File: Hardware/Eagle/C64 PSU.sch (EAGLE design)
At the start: 9 parts

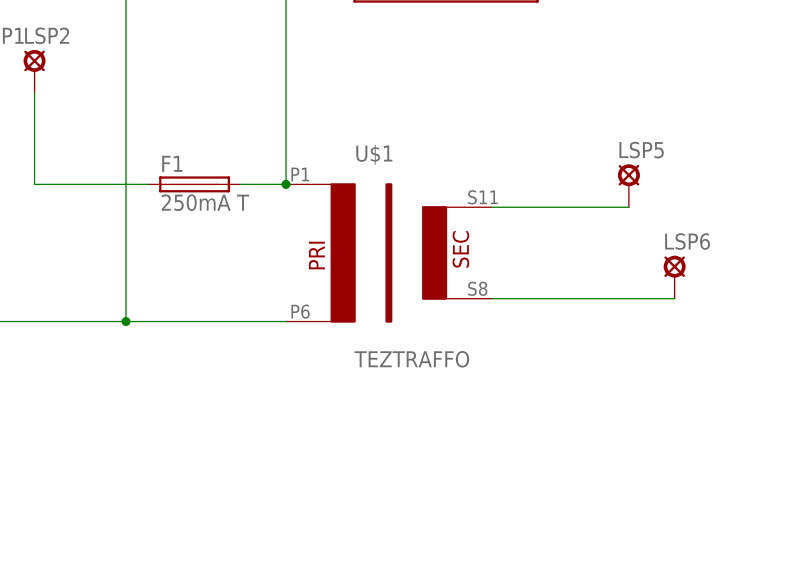
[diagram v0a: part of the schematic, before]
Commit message: Fixed solder pads for trafo
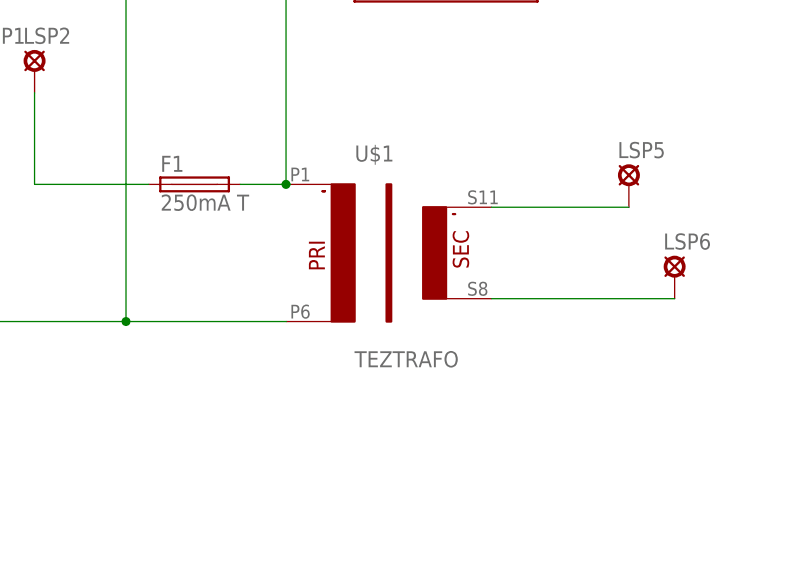
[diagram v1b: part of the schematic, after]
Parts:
- U$1: value TEZTRAFFO -> TEZTRAFO; device traffo:TEZTRAFFO -> trafo:TEZTRAFO
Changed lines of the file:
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@@
 <?xml version="1.0" encoding="utf-8"?>
 <!DOCTYPE eagle SYSTEM "eagle.dtd">
-<eagle version="9.1.3">
+<eagle version="9.2.2">
 <drawing>
 <settings>
@@
 </classes>
 <parts>
-<part name="U$1" library="traffo" deviceset="TEZTRAFFO" device=""/>
+<part name="U$1" library="trafo" deviceset="TEZTRAFO" device=""/>
 <part name="F1" library="fuse" library_urn="urn:adsk.eagle:library:233" deviceset="FUSE" device="SH22,5" package3d_urn="urn:adsk.eagle:package:14059/1" value="250mA T"/>
 <part name="FRAME1" library="frames" library_urn="urn:adsk.eagle:library:229" deviceset="A3L-LOC" device=""/>

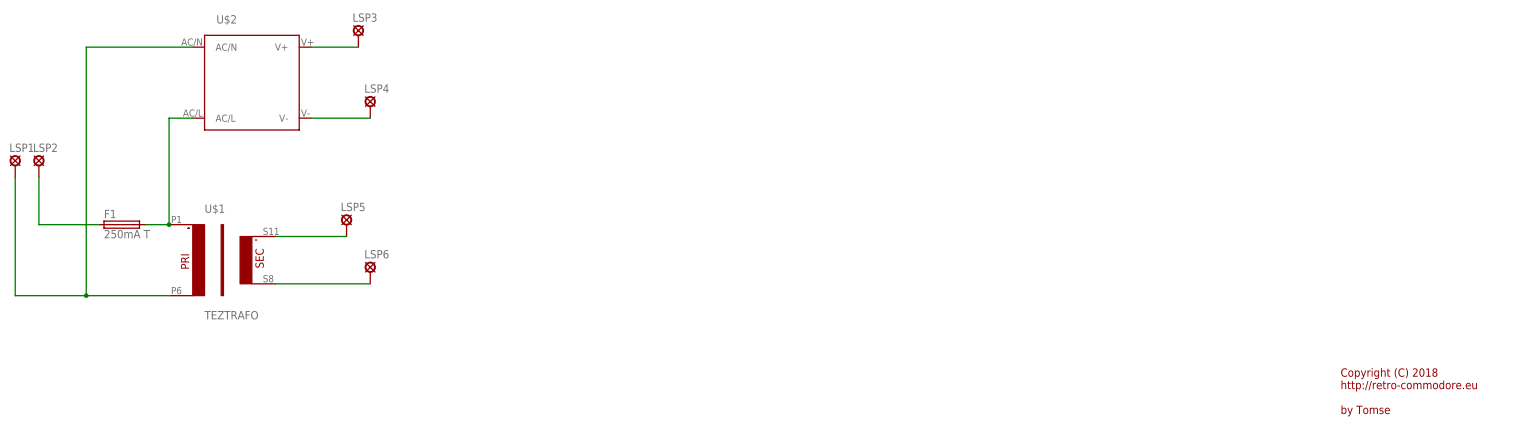
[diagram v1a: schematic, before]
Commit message: added power led connectors
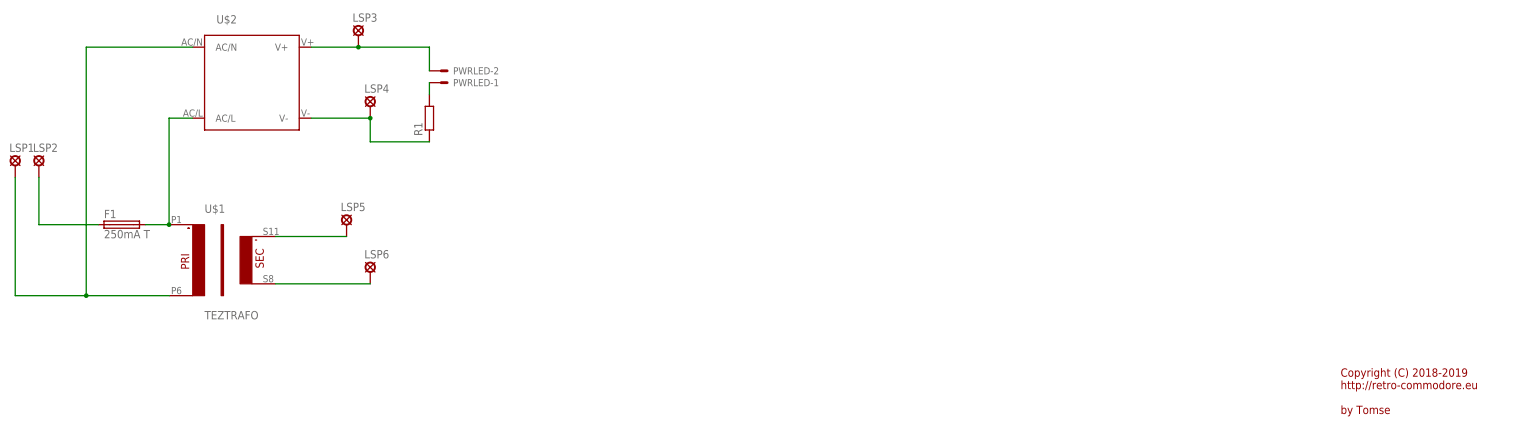
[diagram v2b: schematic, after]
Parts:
- added PWRLED: 22-23-2021, con-molex:22-23-2021
- added R1: (no value), rcl:R-EU_0207/10
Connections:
- new net N$8: PWRLED-1.S, R1.2
- net N$6: now also R1.1
- net N$7: now also PWRLED-2.S
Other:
- note added: "Copyright (C) 2018-2019 http://retro-commodore.eu by Tomse"
- note removed: "Copyright (C) 2018 http://retro-commodore.eu by Tomse"
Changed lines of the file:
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@@
 <?xml version="1.0" encoding="utf-8"?>
 <!DOCTYPE eagle SYSTEM "eagle.dtd">
-<eagle version="9.2.2">
+<eagle version="9.3.2">
 <drawing>
 <settings>
@@
 <grid distance="0.1" unitdist="inch" unit="inch" style="lines" multiple="1" display="no" altdistance="0.01" altunitdist="inch" altunit="inch"/>
 <layers>
-<layer number="1" name="Top" color="4" fill="1" visible="no" active="no"/>
-<layer number="16" name="Bottom" color="1" fill="1" visible="no" active="no"/>
-<layer number="17" name="Pads" color="2" fill="1" visible="no" active="no"/>
-<layer number="18" name="Vias" color="2" fill="1" visible="no" active="no"/>
-<layer number="19" name="Unrouted" color="6" fill="1" visible="no" active="no"/>
-<layer number="20" name="Dimension" color="24" fill="1" visible="no" active="no"/>
-<layer number="21" name="tPlace" color="7" fill="1" visible="no" active="no"/>
-<layer number="22" name="bPlace" color="7" fill="1" visible="no" active="no"/>
-<layer number="23" name="tOrigins" color="15" fill="1" visible="no" active="no"/>
-<layer number="24" name="bOrigins" color="15" fill="1" visible="no" active="no"/>
-<layer number="25" name="tNames" color="7" fill="1" visible="no" active="no"/>
-<layer number="26" name="bNames" color="7" fill="1" visible="no" active="no"/>
-<layer number="27" name="tValues" color="7" fill="1" visible="no" active="no"/>
-<layer number="28" name="bValues" color="7" fill="1" visible="no" active="no"/>
+<layer number="1" name="Top" color="4" fill="1" visible="yes" active="no"/>
+<layer number="16" name="Bottom" color="1" fill="1" visible="yes" active="no"/>
+<layer number="17" name="Pads" color="2" fill="1" visible="yes" active="no"/>
+<layer number="18" name="Vias" color="2" fill="1" visible="yes" active="no"/>
+<layer number="19" name="Unrouted" color="6" fill="1" visible="yes" active="no"/>
+<layer number="20" name="Dimension" color="24" fill="1" visible="yes" active="no"/>
+<layer number="21" name="tPlace" color="7" fill="1" visible="yes" active="no"/>
+<layer number="22" name="bPlace" color="7" fill="1" visible="yes" active="no"/>
+<layer number="23" name="tOrigins" color="15" fill="1" visible="yes" active="no"/>
+<layer number="24" name="bOrigins" color="15" fill="1" visible="yes" active="no"/>
+<layer number="25" name="tNames" color="7" fill="1" visible="yes" active="no"/>
+<layer number="26" name="bNames" color="7" fill="1" visible="yes" active="no"/>
+<layer number="27" name="tValues" color="7" fill="1" visible="yes" active="no"/>
+<layer number="28" name="bValues" color="7" fill="1" visible="yes" active="no"/>
 <layer number="29" name="tStop" color="7" fill="3" visible="no" active="no"/>
 <layer number="30" name="bStop" color="7" fill="6" visible="no" active="no"/>
@@
 <layer number="35" name="tGlue" color="7" fill="4" visible="no" active="no"/>
 <layer number="36" name="bGlue" color="7" fill="5" visible="no" active="no"/>
-<layer number="37" name="tTest" color="7" fill="1" visible="no" active="no"/>
-<layer number="38" name="bTest" color="7" fill="1" visible="no" active="no"/>
+<layer number="37" name="tTest" color="7" fill="1" visible="yes" active="no"/>
+<layer number="38" name="bTest" color="7" fill="1" visible="yes" active="no"/>
 <layer number="39" name="tKeepout" color="4" fill="11" visible="no" active="no"/>
 <layer number="40" name="bKeepout" color="1" fill="11" visible="no" active="no"/>
@@
 <layer number="44" name="Drills" color="7" fill="1" visible="no" active="no"/>
 <layer number="45" name="Holes" color="7" fill="1" visible="no" active="no"/>
-<layer number="46" name="Milling" color="3" fill="1" visible="no" active="no"/>
-<layer number="47" name="Measures" color="7" fill="1" visible="no" active="no"/>
-<layer number="48" name="Document" color="7" fill="1" visible="no" active="no"/>
-<layer number="49" name="Reference" color="7" fill="1" visible="no" active="no"/>
-<layer number="51" name="tDocu" color="7" fill="1" visible="no" active="no"/>
-<layer number="52" name="bDocu" color="7" fill="1" visible="no" active="no"/>
+<layer number="46" name="Milling" color="3" fill="1" visible="yes" active="no"/>
+<layer number="47" name="Measures" color="7" fill="1" visible="yes" active="no"/>
+<layer number="48" name="Document" color="7" fill="1" visible="yes" active="no"/>
+<layer number="49" name="Reference" color="7" fill="1" visible="yes" active="no"/>
+<layer number="51" name="tDocu" color="7" fill="1" visible="yes" active="no"/>
+<layer number="52" name="bDocu" color="7" fill="1" visible="yes" active="no"/>
 <layer number="88" name="SimResults" color="9" fill="1" visible="yes" active="yes"/>
 <layer number="89" name="SimProbes" color="9" fill="1" visible="yes" active="yes"/>
@@
 <part name="LSP5" library="solpad" library_urn="urn:adsk.eagle:library:364" deviceset="SE14" device="" package3d_urn="urn:adsk.eagle:package:26504/1"/>
 <part name="LSP6" library="solpad" library_urn="urn:adsk.eagle:library:364" deviceset="SE14" device="" package3d_urn="urn:adsk.eagle:package:26504/1"/>
+<part name="R1" library="rcl" library_urn="urn:adsk.eagle:library:334" deviceset="R-EU_" device="0207/10" package3d_urn="urn:adsk.eagle:package:23491/2"/>
+<part name="PWRLED" library="con-molex" deviceset="22-23-2021" device="" package3d_urn="urn:adsk.eagle:package:8078633/1"/>
 </parts>
 <sheets>
 <sheet>
 <plain>
-<text x="271.78" y="7.62" size="1.778" layer="94">Copyright (C) 2018
+<text x="271.78" y="7.62" size="1.778" layer="94">Copyright (C) 2018-2019
 http://retro-commodore.eu
 by Tomse</text>
@@
 <instance part="LSP6" gate="1" x="63.5" y="38.1" smashed="yes">
 <attribute name="NAME" x="62.23" y="41.021" size="1.778" layer="95"/>
+</instance>
+<instance part="R1" gate="G$1" x="76.2" y="71.12" smashed="yes" rot="R90">
+<attribute name="NAME" x="74.7014" y="67.31" size="1.778" layer="95" rot="R90"/>
+<attribute name="VALUE" x="79.502" y="67.31" size="1.778" layer="96" rot="R90"/>
+</instance>
+<instance part="PWRLED" gate="-1" x="78.74" y="78.74" smashed="yes">
+<attribute name="NAME" x="81.28" y="77.978" size="1.524" layer="95"/>
+</instance>
+<instance part="PWRLED" gate="-2" x="78.74" y="81.28" smashed="yes">
+<attribute name="NAME" x="81.28" y="80.518" size="1.524" layer="95"/>
 </instance>
 </instances>
@@
 <pinref part="LSP4" gate="1" pin="MP"/>
 <wire x1="50.8" y1="71.12" x2="63.5" y2="71.12" width="0.1524" layer="91"/>
+<wire x1="63.5" y1="71.12" x2="63.5" y2="66.04" width="0.1524" layer="91"/>
+<junction x="63.5" y="71.12"/>
+<wire x1="63.5" y1="66.04" x2="76.2" y2="66.04" width="0.1524" layer="91"/>
+<pinref part="R1" gate="G$1" pin="1"/>
 </segment>
 </net>
@@
 <pinref part="LSP3" gate="1" pin="MP"/>
 <wire x1="50.8" y1="86.36" x2="60.96" y2="86.36" width="0.1524" layer="91"/>
+<wire x1="60.96" y1="86.36" x2="76.2" y2="86.36" width="0.1524" layer="91"/>
+<junction x="60.96" y="86.36"/>
+<pinref part="PWRLED" gate="-2" pin="S"/>
+<wire x1="76.2" y1="81.28" x2="76.2" y2="86.36" width="0.1524" layer="91"/>
+</segment>
+</net>
+<net name="N$8" class="0">
+<segment>
+<pinref part="R1" gate="G$1" pin="2"/>
+<pinref part="PWRLED" gate="-1" pin="S"/>
+<wire x1="76.2" y1="76.2" x2="76.2" y2="78.74" width="0.1524" layer="91"/>
 </segment>
 </net>
@@
 packages will not be understood (or retained) with this version.
 </note>
+<note version="8.4" severity="warning">
+Since Version 8.4, EAGLE supports properties for SPICE simulation.
+Probes in schematics and SPICE mapping objects found in parts and library devices
+will not be understood with this version. Update EAGLE to the latest version
+for full support of SPICE simulation.
+</note>
 </compatibility>

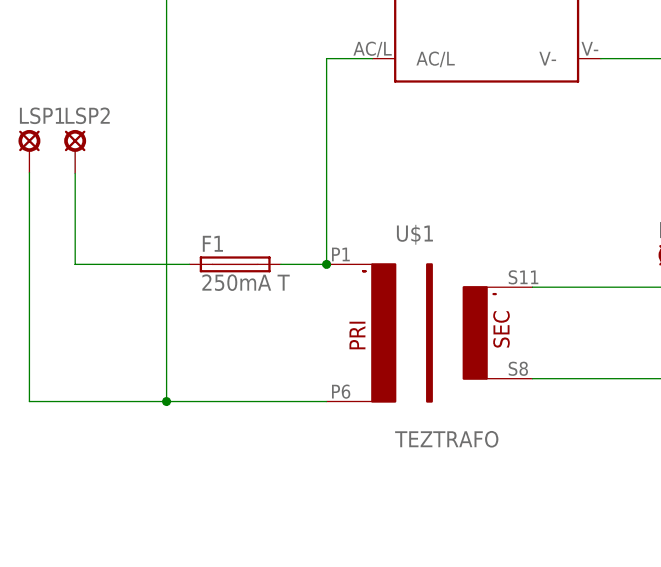
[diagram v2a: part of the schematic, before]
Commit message: Improved traces
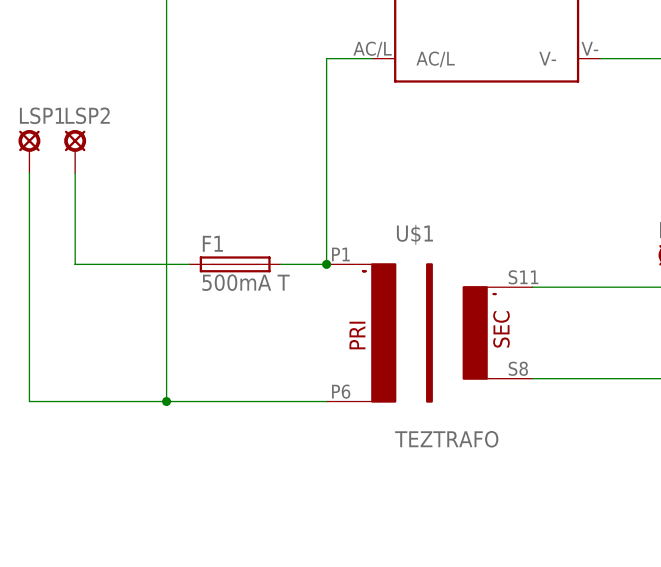
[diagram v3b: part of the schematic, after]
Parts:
- F1: value 250mA T -> 500mA T
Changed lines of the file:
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@@
 <?xml version="1.0" encoding="utf-8"?>
 <!DOCTYPE eagle SYSTEM "eagle.dtd">
-<eagle version="9.3.2">
+<eagle version="9.4.2">
 <drawing>
 <settings>
@@
 <grid distance="0.1" unitdist="inch" unit="inch" style="lines" multiple="1" display="no" altdistance="0.01" altunitdist="inch" altunit="inch"/>
 <layers>
-<layer number="1" name="Top" color="4" fill="1" visible="yes" active="no"/>
-<layer number="16" name="Bottom" color="1" fill="1" visible="yes" active="no"/>
-<layer number="17" name="Pads" color="2" fill="1" visible="yes" active="no"/>
-<layer number="18" name="Vias" color="2" fill="1" visible="yes" active="no"/>
-<layer number="19" name="Unrouted" color="6" fill="1" visible="yes" active="no"/>
-<layer number="20" name="Dimension" color="24" fill="1" visible="yes" active="no"/>
-<layer number="21" name="tPlace" color="7" fill="1" visible="yes" active="no"/>
-<layer number="22" name="bPlace" color="7" fill="1" visible="yes" active="no"/>
-<layer number="23" name="tOrigins" color="15" fill="1" visible="yes" active="no"/>
-<layer number="24" name="bOrigins" color="15" fill="1" visible="yes" active="no"/>
-<layer number="25" name="tNames" color="7" fill="1" visible="yes" active="no"/>
-<layer number="26" name="bNames" color="7" fill="1" visible="yes" active="no"/>
-<layer number="27" name="tValues" color="7" fill="1" visible="yes" active="no"/>
-<layer number="28" name="bValues" color="7" fill="1" visible="yes" active="no"/>
+<layer number="1" name="Top" color="4" fill="1" visible="no" active="no"/>
+<layer number="16" name="Bottom" color="1" fill="1" visible="no" active="no"/>
+<layer number="17" name="Pads" color="2" fill="1" visible="no" active="no"/>
+<layer number="18" name="Vias" color="2" fill="1" visible="no" active="no"/>
+<layer number="19" name="Unrouted" color="6" fill="1" visible="no" active="no"/>
+<layer number="20" name="Dimension" color="24" fill="1" visible="no" active="no"/>
+<layer number="21" name="tPlace" color="7" fill="1" visible="no" active="no"/>
+<layer number="22" name="bPlace" color="7" fill="1" visible="no" active="no"/>
+<layer number="23" name="tOrigins" color="15" fill="1" visible="no" active="no"/>
+<layer number="24" name="bOrigins" color="15" fill="1" visible="no" active="no"/>
+<layer number="25" name="tNames" color="7" fill="1" visible="no" active="no"/>
+<layer number="26" name="bNames" color="7" fill="1" visible="no" active="no"/>
+<layer number="27" name="tValues" color="7" fill="1" visible="no" active="no"/>
+<layer number="28" name="bValues" color="7" fill="1" visible="no" active="no"/>
 <layer number="29" name="tStop" color="7" fill="3" visible="no" active="no"/>
 <layer number="30" name="bStop" color="7" fill="6" visible="no" active="no"/>
@@
 <layer number="35" name="tGlue" color="7" fill="4" visible="no" active="no"/>
 <layer number="36" name="bGlue" color="7" fill="5" visible="no" active="no"/>
-<layer number="37" name="tTest" color="7" fill="1" visible="yes" active="no"/>
-<layer number="38" name="bTest" color="7" fill="1" visible="yes" active="no"/>
+<layer number="37" name="tTest" color="7" fill="1" visible="no" active="no"/>
+<layer number="38" name="bTest" color="7" fill="1" visible="no" active="no"/>
 <layer number="39" name="tKeepout" color="4" fill="11" visible="no" active="no"/>
 <layer number="40" name="bKeepout" color="1" fill="11" visible="no" active="no"/>
@@
 <layer number="44" name="Drills" color="7" fill="1" visible="no" active="no"/>
 <layer number="45" name="Holes" color="7" fill="1" visible="no" active="no"/>
-<layer number="46" name="Milling" color="3" fill="1" visible="yes" active="no"/>
-<layer number="47" name="Measures" color="7" fill="1" visible="yes" active="no"/>
-<layer number="48" name="Document" color="7" fill="1" visible="yes" active="no"/>
-<layer number="49" name="Reference" color="7" fill="1" visible="yes" active="no"/>
-<layer number="51" name="tDocu" color="7" fill="1" visible="yes" active="no"/>
-<layer number="52" name="bDocu" color="7" fill="1" visible="yes" active="no"/>
+<layer number="46" name="Milling" color="3" fill="1" visible="no" active="no"/>
+<layer number="47" name="Measures" color="7" fill="1" visible="no" active="no"/>
+<layer number="48" name="Document" color="7" fill="1" visible="no" active="no"/>
+<layer number="49" name="Reference" color="7" fill="1" visible="no" active="no"/>
+<layer number="51" name="tDocu" color="7" fill="1" visible="no" active="no"/>
+<layer number="52" name="bDocu" color="7" fill="1" visible="no" active="no"/>
 <layer number="88" name="SimResults" color="9" fill="1" visible="yes" active="yes"/>
 <layer number="89" name="SimProbes" color="9" fill="1" visible="yes" active="yes"/>
@@
 <class number="0" name="default" width="0" drill="0">
 </class>
+<class number="1" name="primary" width="0" drill="0">
+<clearance class="0" value="5"/>
+</class>
 </classes>
 <parts>
 <part name="U$1" library="trafo" deviceset="TEZTRAFO" device=""/>
-<part name="F1" library="fuse" library_urn="urn:adsk.eagle:library:233" deviceset="FUSE" device="SH22,5" package3d_urn="urn:adsk.eagle:package:14059/1" value="250mA T"/>
+<part name="F1" library="fuse" library_urn="urn:adsk.eagle:library:233" deviceset="FUSE" device="SH22,5" package3d_urn="urn:adsk.eagle:package:14059/1" value="500mA T"/>
 <part name="FRAME1" library="frames" library_urn="urn:adsk.eagle:library:229" deviceset="A3L-LOC" device=""/>
 <part name="U$2" library="meanwell_irm_v7" deviceset="IRM_15/20" device="IRM_15/20"/>
@@
 </busses>
 <nets>
-<net name="N$1" class="0">
+<net name="N$1" class="1">
 <segment>
 <pinref part="F1" gate="G$1" pin="2"/>
@@
 </segment>
 </net>
-<net name="N$2" class="0">
+<net name="N$2" class="1">
 <segment>
 <pinref part="U$2" gate="G$1" pin="AC/N"/>
@@
 </segment>
 </net>
-<net name="N$3" class="0">
+<net name="N$3" class="1">
 <segment>
 <pinref part="F1" gate="G$1" pin="1"/>
